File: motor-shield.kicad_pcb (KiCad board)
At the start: 4 copper layers, 65.9 x 52.7 mm, 123 parts, among them J101 MC 1,5/ 2-G-3,5, J102 -, J103 MC 1,5/ 2-G-3,5, J104 -, J105 STEMMA QT, J106 Conn_02x04_smd, J107 Conn_01x04_f, J201 -, J202 -, J203 Barrel_Jack_MountingPin, Q101 AO3400A, Q102 AO3400A, Q201 AOD4185, SW101 Switch, U101 74HC04, U102 74HC08, U103 74HC32, U104 DRV8874PWPR, U105 DRV8874PWPR, U106 LMV321, U201 MP9942GJ

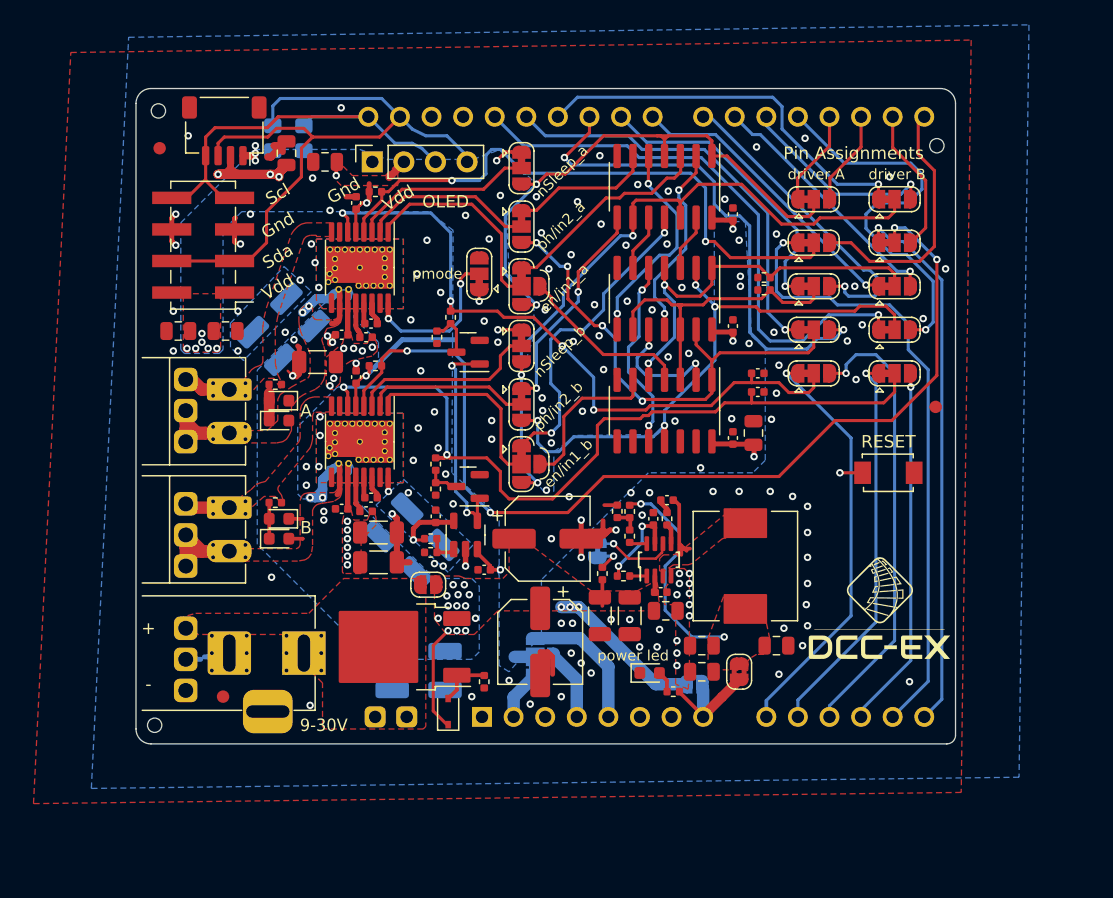
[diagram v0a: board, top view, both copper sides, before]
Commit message: Update to RevA1
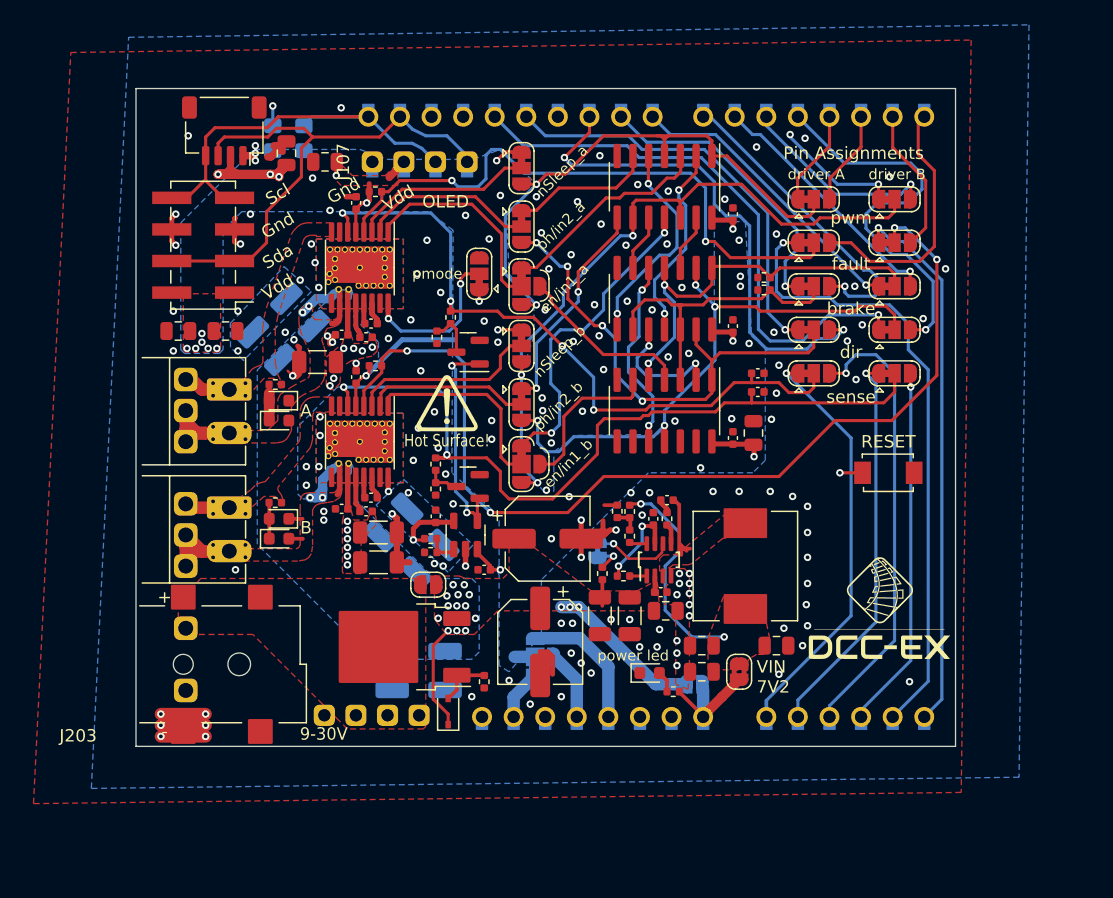
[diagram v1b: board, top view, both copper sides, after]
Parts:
- removed FID101, FID102, FID103: Toolinghole_jlc, _my:toolinghole_jlc
- removed FID104, FID105, FID106: Fiducial, Fiducial:Fiducial_1mm_Mask2mm
- removed the REF** at (120.5, 100.0)
- added G***: LOGO, _my:danger-5mm, F.Cu at (89.0, 83.9)
- added G***: LOGO, _my:EX-8874-QR-20mm, B.Cu at (120.2, 97.4)
- added REF**: KiCad-Logo2_5mm_SilkScreen, Symbol:KiCad-Logo2_5mm_SilkScreen, B.Cu at (72.7, 69.7)
- A101: footprint Module:Arduino_UNO_R3 -> _my:Arduino_UNO_R3_edit
- J107: footprint Connector_PinSocket_2.54mm:PinSocket_1x04_P2.54mm_Vertical -> _my:PinHeader_1x04_P2.54mm_Vertical_solderpad
- J201: footprint _my:PinHeader_1x02_P2.54mm_Vertical_min -> _my:PinHeader_1x04_P2.54mm_Vertical_min_1
- J202: footprint _my:PinHeader_01x03_P2.5mm_Vertical_min -> _my:PinHeader_01x02_P5mm_Vertical_min
- J203: footprint _my:BarrelJack_2.1mm -> _my:BarrelJack_2.1mm_SMD
- moved J203 9.74 mm to (67.8, 104.9)
- moved G*** 3.67 mm to (95.3, 77.4)
- moved J201 3.54 mm to (86.8, 109.0), turned to -90 degrees
- moved G*** 3.52 mm to (117.1, 78.5)
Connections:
- J201 pad 2: /Power/v_conn -> GND
- J203 pad MP: unconnected-(J203-MountPin-PadMP) -> GND
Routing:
- net GND: track 42.1 -> 46.5 mm, vias 153 -> 158
- net /fault_n_a: track 48.1 -> 48.7 mm
- net /sda: vias 0 -> 1
- net /def_pwm_b: vias 1 -> 2
- removed copper zone on In2.Cu, net /Power/v_conn
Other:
- board size 65.9 x 52.7 mm -> 65.9 x 52.9 mm
- board text added: "3V3"
- board text added: "Hot Surface!"
- board text added: "Rev A1"
- board text added: "VIN 7V2"
- board text added: "brake"
- board text added: "dir"
- board text added: "fault"
- board text added: "pwm"
- board text added: "sense"
- board text removed: "3V"
- board text removed: "Rev A"
- board text removed: "RoHS"

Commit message: Rev A2
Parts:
- added R103: 47k, _my:R_1005_(0402), F.Cu at (114.5, 65.6)
- added R104: 47k, _my:R_1005_(0402), F.Cu at (114.5, 69.4)
- JP101, JP102, JP103, JP105, JP106, JP108, JP109, JP110, JP111, JP112, JP113, JP114, JP115, JP116, JP117: footprint Jumper:SolderJumper-3_P1.3mm_Bridged12_RoundedPad1.0x1.5mm -> _my:SolderJumper-3
- JP203: renamed from JP202; footprint Jumper:SolderJumper-2_P1.3mm_Bridged2Bar_RoundedPad1.0x1.5mm -> _my:SolderJumper-2_P1.3mm_Bridged
- JP204: renamed from JP203; footprint Jumper:SolderJumper-2_P1.3mm_Bridged2Bar_RoundedPad1.0x1.5mm -> _my:SolderJumper-2_P1.3mm_Bridged
- moved R110 33.3 mm to (115.9, 87.2)
- moved R109 31.6 mm to (114.5, 71.4)
- moved D103 0.20 mm to (75.5, 94.6)
- moved D104 0.20 mm to (75.5, 93.0)
- moved J103 0.20 mm to (71.5, 92.1)
- moved R108 0.20 mm to (75.2, 91.7)
- renumbered C208 to C201, C209 to C202, C210 to C203, C211 to C204, C212 to C205, C213 to C206, C214 to C207, C215 to C208, C216 to C209, C217 to C210, C218 to C211, C201 to C212, C202 to C213, C203 to C214, C204 to C215, C205 to C216, C206 to C217, C207 to C218, J203 to J201, J201 to J203, JP204 to JP201, JP201 to JP202, R103 to R105, R104 to R106, R105 to R107, R106 to R108, R107 to R109, R108 to R110, R109 to R111, R110 to R112, R111 to R113, R112 to R114, R113 to R115, R114 to R116, R208 to R201, R201 to R202, R202 to R203, R207 to R204, R203 to R205, R204 to R206, R205 to R207, R206 to R208
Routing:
- net GND: track 46.5 -> 48.4 mm, vias 158 -> 164
- net IOREF: track 38.3 -> 39.6 mm
- net /fault_n_b: track 80.0 -> 80.7 mm
- net /pwm_a: track 45.1 -> 45.8 mm
- net /pwm_b: track 56.8 -> 57.4 mm
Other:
- board text added: "Rev A2"
- board text removed: "Rev A1"

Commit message: update to RevB
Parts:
- removed the C206 at (74.5, 79.3)
- removed the C207 at (77.2, 76.6)
- removed the C213 at (106.6, 100.6)
- removed the C218 at (105.6, 93.2)
- removed the R202 at (103.2, 97.8)
- removed R205: 470k, _my:R_1005_(0402)
- removed R206, R207: 47k, _my:R_1005_(0402)
- removed R208: 5k76, _my:R_1005_(0402)
- added C215: 56p, _my:C_1005_(0402), F.Cu at (105.3, 103.6)
- added R204: 9k1, _my:R_1005_(0402), F.Cu at (103.3, 103.6)
- D101, D102, D103, D104: value 0603_LED_Red -> 0603_LED_Yellow
- JP204: value Jumper_2 -> Jumper_2_o; footprint _my:SolderJumper-2_P1.3mm_Bridged -> Jumper:SolderJumper-2_P1.3mm_Open_RoundedPad1.0x1.5mm
- L201: value 56uH -> 15uH; footprint _my:L_PSPMAA0805 -> 0_my:L_7.1x6.6_H3_SLO0630H
- Q201: value AOD4185 -> AO4407C; footprint Package_TO_SOT_SMD:TO-252-2 -> Package_SO:SOIC-8_3.9x4.9mm_P1.27mm
- R115: value 47k -> 9k1
- R116: value 470k -> 100k
- R203: value 20R -> 100k
- U201: value MP9942GJ -> TPS54302; footprint _my:TSOT23-8 -> Package_TO_SOT_SMD:SOT-23-6
- moved C208 11.0 mm to (107.2, 102.7), turned to -90 degrees
- moved R203 10.7 mm to (104.3, 103.6)
- moved D201 10.2 mm to (88.5, 98.5), turned to 180 degrees
- moved R201 9.92 mm to (85.5, 98.8), turned to 180 degrees
- moved JP201 8.00 mm to (87.5, 106.5)
- moved C209 6.00 mm to (103.9, 95.0), turned to 90 degrees
- moved C214 5.73 mm to (109.8, 102.8), turned to 180 degrees
- moved C212 4.81 mm to (109.8, 98.6)
- moved C213 4.81 mm to (109.8, 100.7)
- moved L201 4.81 mm to (109.6, 93.6), turned to 0 degrees
- moved G*** 4.64 mm to (121.4, 97.0)
- moved U201 3.00 mm to (106.1, 99.5), turned to -90 degrees
- moved C211 2.41 mm to (103.8, 98.9), turned to -90 degrees
- moved Q201 1.49 mm to (84.5, 102.5)
- moved C210 1.22 mm to (102.0, 100.0)
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- renumbered C208 to C204, C209 to C205, C210 to C206, C211 to C207, C212 to C208, C205 to C209, C204 to C210, C214 to C211, C215 to C212, C216 to C213, C217 to C214, C219 to C216, C220 to C217, C221 to C218, C222 to C219, C223 to C220, C224 to C221, C225 to C222, R204 to R202
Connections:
- C208 pad 1: Net-(C212-Pad1) -> /Power/bst
- JP204 pad 1: /Power/en -> GND
- Q201 pad 1: /Power/gate -> VM
- Q201 pad 2: /Power/v_conn -> VM
- R203 pad 1: /Power/bst -> /Power/vin
- R203 pad 2: Net-(C212-Pad1) -> /Power/fn
- U201 pad 1: /Power/pg -> GND
- U201 pad 2: VM -> /Power/sw
- U201 pad 3: /Power/sw -> VM
- U201 pad 4: GND -> /Power/fn
- U201 pad 5: /Power/bst -> /Power/en2
- U201 pad 6: /Power/en2 -> /Power/bst
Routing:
- net GND: track 48.4 -> 111.6 mm, vias 164 -> 159
- net VM: track 30.6 -> 19.1 mm, vias 28 -> 27
- net /Power/vin: track 17.3 -> 9.55 mm
- net /Power/vcc: track 7.29 -> 0.00 mm, vias 2 -> 0
- net /Power/en: track 2.82 -> 0.00 mm, vias 1 -> 0
- net /Power/fn: track 2.08 -> 4.31 mm
- net /Power/en2: track 6.85 -> 8.42 mm
- net /Power/fb: track 1.28 -> 0.00 mm
- net /Power/pg: track 1.28 -> 0.00 mm
- net Net-(C212-Pad1): track 1.21 -> 0.00 mm
- net /Power/sw: track 6.84 -> 7.72 mm, vias 0 -> 2
- net /Power/gate: track 4.34 -> 3.57 mm
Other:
- board text added: "(Prog.)"
- board text added: "9-25V"
- board text added: "DCC-EX.com"
- board text added: "EX-Motorshield8874"
- board text added: "Regulator Disable"
- board text added: "RevB2 S/N:___________"
- board text removed: "9-30V"
- board text removed: "DRV8874"
- board text removed: "PRIVATE USE"
- board text removed: "Regulator Enable"
- board text removed: "Rev A2"
- board text removed: "S/N:___________"
- board text removed: "VIN 7V2"
